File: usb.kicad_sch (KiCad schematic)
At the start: 7 parts, among them J5 USB, U6 USBLC6-2SC6

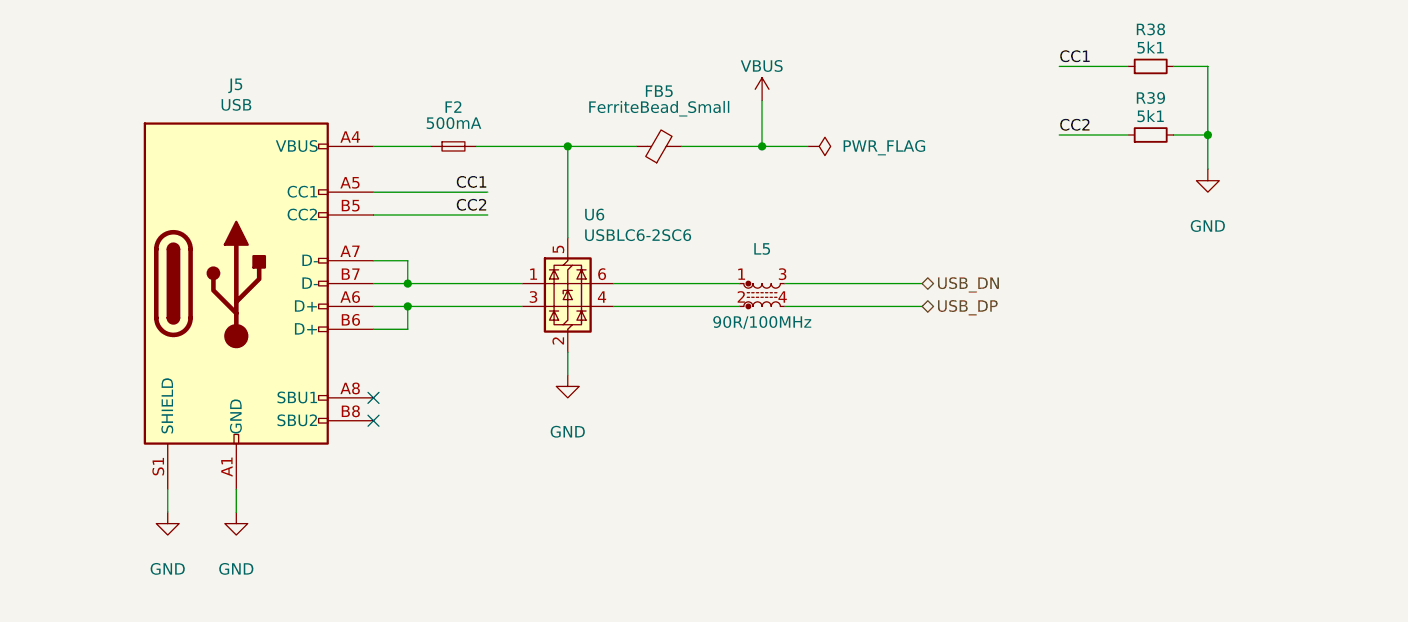
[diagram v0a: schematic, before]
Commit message: sch: fixing component footprints
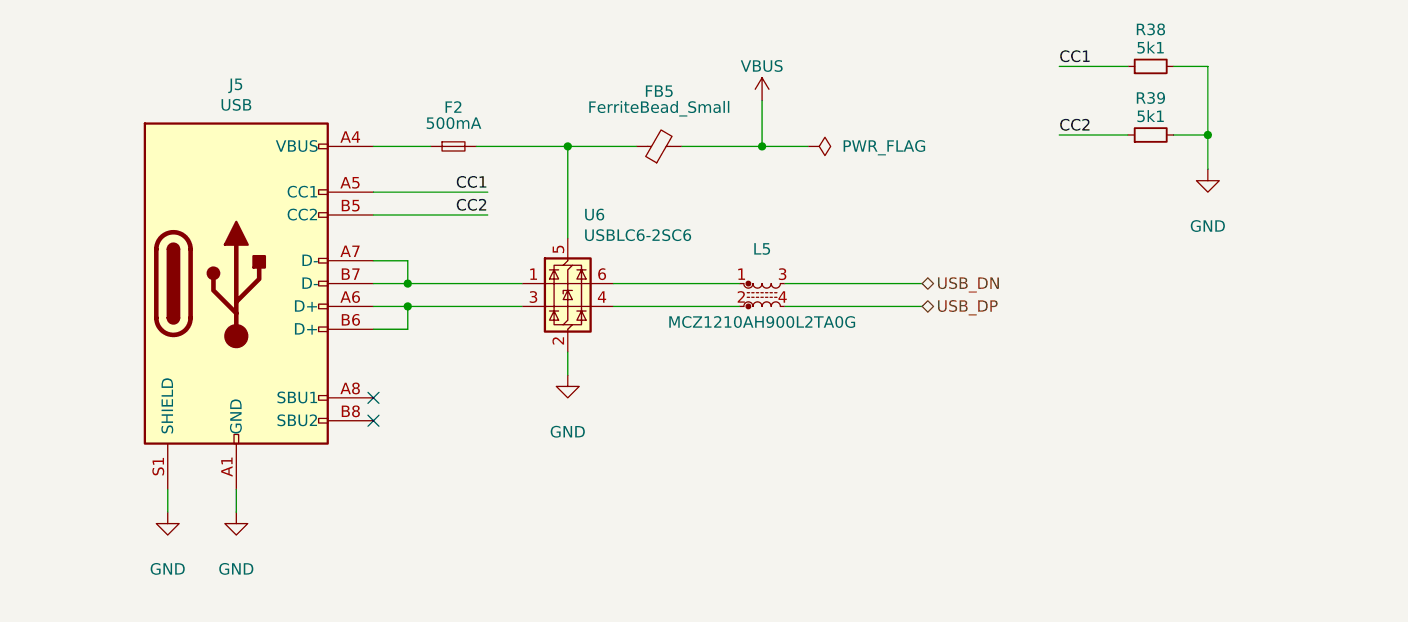
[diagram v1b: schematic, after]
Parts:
- F2: footprint (none) -> Fuse:Fuse_1206_3216Metric
- FB5: footprint (none) -> Inductor_SMD:L_0805_2012Metric_Pad1.05x1.20mm_HandSolder
- L5: value 90R/100MHz -> MCZ1210AH900L2TA0G; footprint (none) -> MCZ1210AH900L2TA0G:MCZ1210AH201L2TA0G
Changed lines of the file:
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@@
 			)
 		)
-		(property "Footprint" ""
+		(property "Footprint" "Inductor_SMD:L_0805_2012Metric_Pad1.05x1.20mm_HandSolder"
 			(at 148.59 83.058 90)
 			(effects
@@
 			)
 		)
-		(property "Footprint" ""
+		(property "Footprint" "Fuse:Fuse_1206_3216Metric"
 			(at 125.73 81.28 0)
 			(effects
@@
 			)
 		)
-		(property "Value" "90R/100MHz"
+		(property "Value" "MCZ1210AH900L2TA0G"
 			(at 160.02 100.838 0)
 			(effects
@@
 			)
 		)
-		(property "Footprint" ""
+		(property "Footprint" "MCZ1210AH900L2TA0G:MCZ1210AH201L2TA0G"
 			(at 160.02 97.79 0)
 			(effects

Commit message: brd: routing in progress
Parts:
- removed F2: 500mA, Fuse:Fuse_1206_3216Metric, symbol Device:Fuse_Small
- removed FB5: FerriteBead_Small, Inductor_SMD:L_0805_2012Metric_Pad1.05x1.20mm_HandSolder, symbol Device:FerriteBead_Small
- added TP3: V_{BUS}, TestPoint:TestPoint_Pad_D1.0mm, symbol Connector:TestPoint
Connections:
- net USB_DN: now also L5.4; no longer L5.3
- net USB_DP: now also L5.3; no longer L5.4
- net VBUS: now also J5.A4 (VBUS), J5.A9 (VBUS), J5.B4 (VBUS), J5.B9 (VBUS), U6.5 (VBUS), TP3.1
- net USB_CONN_DN: now reaches J5.A7 (D-), J5.B7 (D-)
- net USB_CONN_DN: now also U6.3 (I/O2); no longer U6.1 (I/O1)
- net USB_CONN_DP: now reaches J5.A6 (D+), J5.B6 (D+)
- net USB_CONN_DP: now also U6.1 (I/O1); no longer U6.3 (I/O2)
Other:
- moved on the sheet: J5, L5, R38, R39, U6
